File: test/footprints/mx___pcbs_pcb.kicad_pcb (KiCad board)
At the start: 2 copper layers, 5 parts

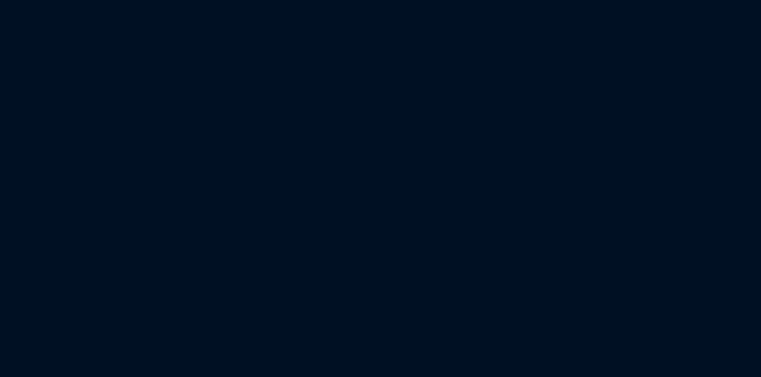
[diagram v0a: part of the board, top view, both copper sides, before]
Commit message: expand code coverage for `mx` footprint
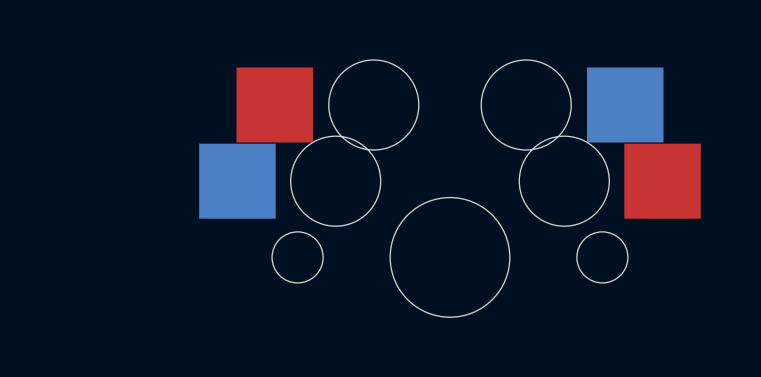
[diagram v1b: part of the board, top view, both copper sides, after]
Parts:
- added S6: , MX, F.Cu at (250.0, 0.00)
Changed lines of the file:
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@@
+        (pad 2 smd rect (at -5.842 -5.08 0) (size 2.55 2.5) (layers F.Cu F.Paste F.Mask) (net 2 "to"))
+        )
+      (module MX (layer F.Cu)
+      (at 250 0 0)
+      (fp_text reference "S6" (at 0 0) (layer F.SilkS) hide (effects (font (size 1.27 1.27) (thickness 0.15))))
+      (fp_text value "" (at 0 0) (layer F.SilkS) hide (effects (font (size 1.27 1.27) (thickness 0.15))))
+      (fp_line (start -7 -6) (end -7 -7) (layer Dwgs.User) (width 0.15))
+      (fp_line (start -7 7) (end -6 7) (layer Dwgs.User) (width 0.15))
+      (fp_line (start -6 -7) (end -7 -7) (layer Dwgs.User) (width 0.15))
+      (fp_line (start -7 7) (end -7 6) (layer Dwgs.User) (width 0.15))
+      (fp_line (start 7 6) (end 7 7) (layer Dwgs.User) (width 0.15))
+      (fp_line (start 7 -7) (end 6 -7) (layer Dwgs.User) (width 0.15))
+      (fp_line (start 6 7) (end 7 7) (layer Dwgs.User) (width 0.15))
+      (fp_line (start 7 -7) (end 7 -6) (layer Dwgs.User) (width 0.15))
+      (pad "" np_thru_hole circle (at 0 0) (size 3.9878 3.9878) (drill 3.9878) (layers *.Cu *.Mask))
+      (pad "" np_thru_hole circle (at 5.08 0) (size 1.7018 1.7018) (drill 1.7018) (layers *.Cu *.Mask))
+      (pad "" np_thru_hole circle (at -5.08 0) (size 1.7018 1.7018) (drill 1.7018) (layers *.Cu *.Mask))
+      (fp_line (start -9.5 -9.5) (end 9.5 -9.5) (layer Dwgs.User) (width 0.15))
+      (fp_line (start 9.5 -9.5) (end 9.5 9.5) (layer Dwgs.User) (width 0.15))
+      (fp_line (start 9.5 9.5) (end -9.5 9.5) (layer Dwgs.User) (width 0.15))
+      (fp_line (start -9.5 9.5) (end -9.5 -9.5) (layer Dwgs.User) (width 0.15))
+        (pad "" np_thru_hole circle (at 2.54 -5.08) (size 3 3) (drill 3) (layers *.Cu *.Mask))
+        (pad "" np_thru_hole circle (at -3.81 -2.54) (size 3 3) (drill 3) (layers *.Cu *.Mask))
+        (pad 1 smd rect (at -7.085 -2.54 0) (size 2.55 2.5) (layers B.Cu B.Paste B.Mask) (net 1 "from"))
+        (pad 2 smd rect (at 5.842 -5.08 0) (size 2.55 2.5) (layers B.Cu B.Paste B.Mask) (net 2 "to"))
+        (pad "" np_thru_hole circle (at -2.54 -5.08) (size 3 3) (drill 3) (layers *.Cu *.Mask))
+        (pad "" np_thru_hole circle (at 3.81 -2.54) (size 3 3) (drill 3) (layers *.Cu *.Mask))
+        (pad 1 smd rect (at 7.085 -2.54 0) (size 2.55 2.5) (layers F.Cu F.Paste F.Mask) (net 1 "from"))
         (pad 2 smd rect (at -5.842 -5.08 0) (size 2.55 2.5) (layers F.Cu F.Paste F.Mask) (net 2 "to"))
         )
